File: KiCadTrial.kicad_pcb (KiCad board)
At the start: 2 copper layers, 3 parts, among them J1 Conn_01x02

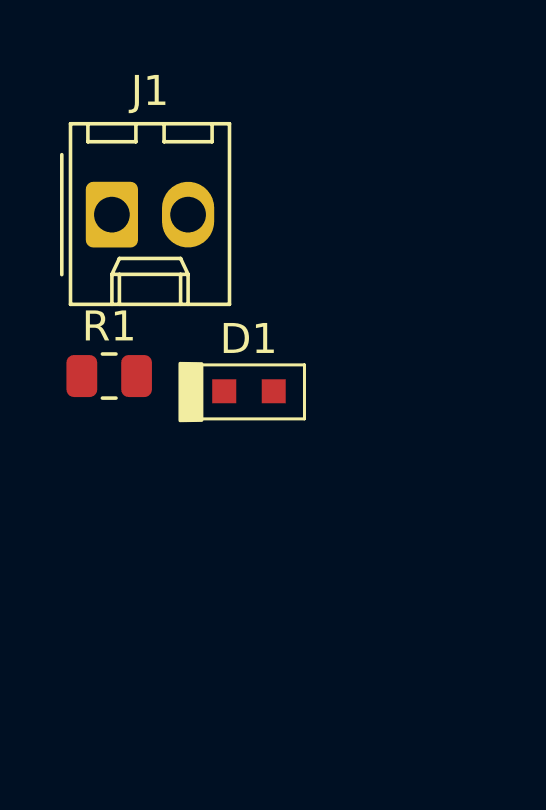
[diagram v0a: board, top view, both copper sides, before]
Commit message: Initial PCB Routing
Placed component on grid.
Routed copper on the front layer.
Defined a board outline.
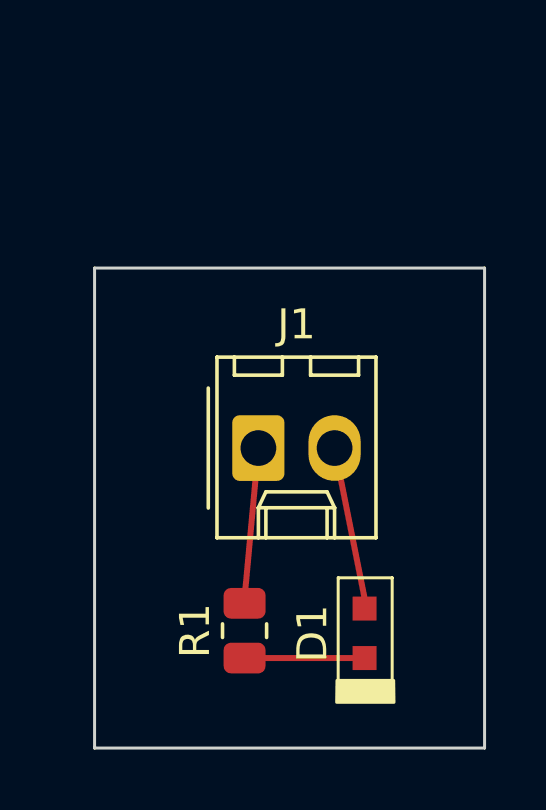
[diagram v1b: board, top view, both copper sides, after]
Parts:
- moved R1 9.61 mm to (156.0, 110.1), turned to 90 degrees
- moved J1 9.19 mm to (156.5, 104.0)
- moved D1 8.94 mm to (160.0, 110.2), turned to 90 degrees
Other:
- board outline added: 13 x 16 mm
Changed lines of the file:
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@@
   (net 3 "+3.3V")
   (footprint "myPCBLib:LED0603" (layer "F.Cu")
-    (at 156.147 102.108)
+    (at 160 110.175 90)
     (descr "Surface Mount LED 0603 - white")
     (tags "optical electronics")
@@
     (property "ki_keywords" "Optoelectronics")
     (attr smd)
-    (fp_text reference "D1" (at -0.01 -1.74 unlocked) (layer "F.SilkS")
+    (fp_text reference "D1" (at -0.01 -1.74 90 unlocked) (layer "F.SilkS")
         (effects (font (size 1 1) (thickness 0.1)))
     )
-    (fp_text value "White" (at 0.03 2.37 unlocked) (layer "F.Fab")
-        (effects (font (size 1 1) (thickness 0.15)))
-    )
-    (fp_text user "REF**" (at -2.11 0.69 unlocked) (layer "F.Fab")
+    (fp_text value "White" (at 0.03 2.37 90 unlocked) (layer "F.Fab")
+        (effects (font (size 1 1) (thickness 0.15)))
+    )
+    (fp_text user "REF**" (at -2.11 0.69 90 unlocked) (layer "F.Fab")
         (effects (font (size 1 1) (thickness 0.15)) (justify left bottom))
     )
-    (fp_text user "${REFERENCE}" (at 0 1.54 unlocked) (layer "F.Fab")
+    (fp_text user "${REFERENCE}" (at 0 1.54 90 unlocked) (layer "F.Fab")
         (effects (font (size 0.5 0.5) (thickness 0.125)))
     )
@@
       )
       (stroke (width 0.1) (type solid)) (fill solid) (layer "F.CrtYd"))
-    (pad "A" smd rect (at 0.825 0) (size 0.8 0.8) (layers "F.Cu" "F.Paste" "F.Mask")
+    (pad "A" smd rect (at 0.825 0 90) (size 0.8 0.8) (layers "F.Cu" "F.Paste" "F.Mask")
       (net 1 "GND") (pinfunction "Anode") (pintype "passive") (thermal_bridge_angle 45))
-    (pad "C" smd rect (at -0.825 0) (size 0.8 0.8) (layers "F.Cu" "F.Paste" "F.Mask")
+    (pad "C" smd rect (at -0.825 0 90) (size 0.8 0.8) (layers "F.Cu" "F.Paste" "F.Mask")
       (net 2 "Net-(D1-Cathode)") (pinfunction "Cathode") (pintype "passive") (thermal_bridge_angle 45))
     (model "${KICAD6_3DMODEL_DIR}/LED_SMD.3dshapes/LED_0603_1608Metric.wrl"
@@
   )
   (footprint "Connector_Molex:Molex_KK-254_AE-6410-02A_1x02_P2.54mm_Vertical" (layer "F.Cu")
-    (at 151.5775 96.22)
+    (at 156.46 104)
     (descr "Molex KK-254 Interconnect System, old/engineering part number: AE-6410-02A example for new part number: 22-27-2021, 2 Pins (http://www.molex.com/pdm_docs/sd/022272021_sd.pdf), generated with kicad-footprint-generator")
     (tags "connector Molex KK-254 vertical")
@@
   )
   (footprint "Resistor_SMD:R_0805_2012Metric" (layer "F.Cu")
-    (at 151.4875 101.6)
+    (at 156 110.0875 90)
     (descr "Resistor SMD 0805 (2012 Metric), square (rectangular) end terminal, IPC_7351 nominal, (Body size source: IPC-SM-782 page 72, https://www.pcb-3d.com/wordpress/wp-content/uploads/ipc-sm-782a_amendment_1_and_2.pdf), generated with kicad-footprint-generator")
     (tags "resistor")
@@
     (property "ki_keywords" "resistor variable light sensitive opto LDR")
     (attr smd)
-    (fp_text reference "R1" (at 0 -1.65) (layer "F.SilkS")
-        (effects (font (size 1 1) (thickness 0.15)))
-    )
-    (fp_text value "R_Photo" (at 0 1.65) (layer "F.Fab")
-        (effects (font (size 1 1) (thickness 0.15)))
-    )
-    (fp_text user "${REFERENCE}" (at 0 0) (layer "F.Fab")
+    (fp_text reference "R1" (at 0 -1.65 90) (layer "F.SilkS")
+        (effects (font (size 1 1) (thickness 0.15)))
+    )
+    (fp_text value "R_Photo" (at 0 1.65 90) (layer "F.Fab")
+        (effects (font (size 1 1) (thickness 0.15)))
+    )
+    (fp_text user "${REFERENCE}" (at 0 0 90) (layer "F.Fab")
         (effects (font (size 0.5 0.5) (thickness 0.08)))
     )
@@
     (fp_line (start 1 0.625) (end -1 0.625)
       (stroke (width 0.1) (type solid)) (layer "F.Fab"))
-    (pad "1" smd roundrect (at -0.9125 0) (size 1.025 1.4) (layers "F.Cu" "F.Paste" "F.Mask") (roundrect_rratio 0.243902)
+    (pad "1" smd roundrect (at -0.9125 0 90) (size 1.025 1.4) (layers "F.Cu" "F.Paste" "F.Mask") (roundrect_rratio 0.243902)
       (net 2 "Net-(D1-Cathode)") (pintype "passive"))
-    (pad "2" smd roundrect (at 0.9125 0) (size 1.025 1.4) (layers "F.Cu" "F.Paste" "F.Mask") (roundrect_rratio 0.243902)
+    (pad "2" smd roundrect (at 0.9125 0 90) (size 1.025 1.4) (layers "F.Cu" "F.Paste" "F.Mask") (roundrect_rratio 0.243902)
       (net 3 "+3.3V") (pintype "passive"))
     (model "${KICAD6_3DMODEL_DIR}/Resistor_SMD.3dshapes/R_0805_2012Metric.wrl"
@@
     )
   )
+  (gr_line (start 160 109) (end 159 104)
+    (stroke (width 0.2) (type default)) (layer "F.Cu"))
+  (gr_line (start 156 109) (end 156.46 104)
+    (stroke (width 0.2) (type default)) (layer "F.Cu"))
+  (gr_line (start 160 111) (end 156 111)
+    (stroke (width 0.2) (type default)) (layer "F.Cu"))
+  (gr_line (start 164 98) (end 164 114)
+    (stroke (width 0.1) (type default)) (layer "Edge.Cuts"))
+  (gr_line (start 164 114) (end 151 114)
+    (stroke (width 0.1) (type default)) (layer "Edge.Cuts"))
+  (gr_line (start 151 114) (end 151 98)
+    (stroke (width 0.1) (type default)) (layer "Edge.Cuts"))
+  (gr_line (start 151 98) (end 164 98)
+    (stroke (width 0.1) (type default)) (layer "Edge.Cuts"))
 )

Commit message: Changes by Lee.
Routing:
- net GND: track 0.00 -> 6.07 mm
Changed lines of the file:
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@@
     )
   )
-  (gr_line (start 160 109) (end 159 104)
-    (stroke (width 0.2) (type default)) (layer "F.Cu"))
   (gr_line (start 156 109) (end 156.46 104)
     (stroke (width 0.2) (type default)) (layer "F.Cu"))
@@
   (gr_line (start 151 98) (end 164 98)
     (stroke (width 0.1) (type default)) (layer "Edge.Cuts"))
+  (segment (start 160.02 104.521) (end 160 104.541) (width 0.25) (layer "F.Cu") (net 1))
+  (segment (start 159.499 104) (end 160.02 104.521) (width 0.25) (layer "F.Cu") (net 1))
+  (segment (start 160 104.541) (end 160 109.35) (width 0.25) (layer "F.Cu") (net 1))
+  (segment (start 159 104) (end 159.499 104) (width 0.25) (layer "F.Cu") (net 1))
 )

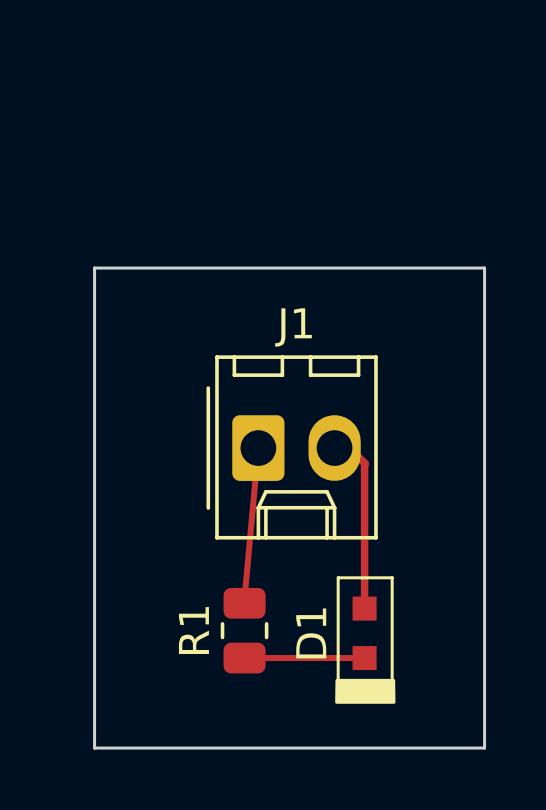
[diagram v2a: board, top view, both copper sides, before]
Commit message: Add ground fill to the Front Copper
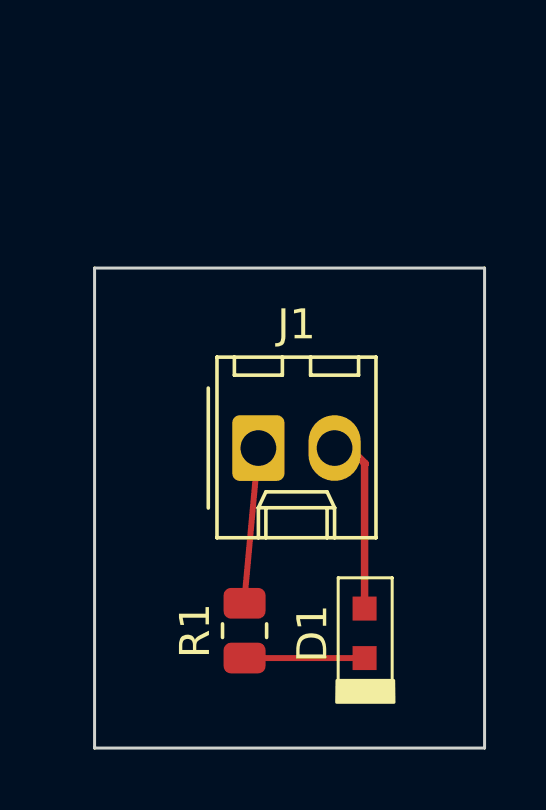
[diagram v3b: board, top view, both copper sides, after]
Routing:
- added copper zone on F.Cu, net GND
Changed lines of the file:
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@@
   (segment (start 160 104.541) (end 160 109.35) (width 0.25) (layer "F.Cu") (net 1))
   (segment (start 159 104) (end 159.499 104) (width 0.25) (layer "F.Cu") (net 1))
+  (zone (net 1) (net_name "GND") (layer "F.Cu") (hatch edge 0.5)
+    (connect_pads (clearance 0.5))
+    (min_thickness 0.25) (filled_areas_thickness no)
+    (fill yes (thermal_gap 0.5) (thermal_bridge_width 0.5))
+    (polygon
+      (pts
+        (xy 151 98)
+        (xy 164 98)
+        (xy 164 114)
+        (xy 151 114)
+      )
+    )
+  )
 )

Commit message: JLCPCB PN
added JLCPCB PN to all components.
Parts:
- R1: value R_Photo -> 330
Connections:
- D1 pad C: Net-(D1-Cathode) -> unconnected-(D1-Cathode-PadC)
- R1 pad 1: Net-(D1-Cathode) -> unconnected-(R1-Pad1)
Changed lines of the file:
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@@
   (net 0 "")
   (net 1 "GND")
-  (net 2 "Net-(D1-Cathode)")
+  (net 2 "unconnected-(D1-Cathode-PadC)")
   (net 3 "+3.3V")
+  (net 4 "unconnected-(R1-Pad1)")
   (footprint "myPCBLib:LED0603" (layer "F.Cu")
     (at 160 110.175 90)
     (descr "Surface Mount LED 0603 - white")
     (tags "optical electronics")
+    (property "JLCPCB" "C965805")
+    (property "MPN" "XL-1608SYGC-06")
+    (property "Manufacturer" "XINGLIGHT")
     (property "PN" "EKT_426738")
     (property "Sheetfile" "KiCadTrial.kicad_sch")
@@
       (net 1 "GND") (pinfunction "Anode") (pintype "passive") (thermal_bridge_angle 45))
     (pad "C" smd rect (at -0.825 0 90) (size 0.8 0.8) (layers "F.Cu" "F.Paste" "F.Mask")
-      (net 2 "Net-(D1-Cathode)") (pinfunction "Cathode") (pintype "passive") (thermal_bridge_angle 45))
+      (net 2 "unconnected-(D1-Cathode-PadC)") (pinfunction "Cathode") (pintype "passive") (thermal_bridge_angle 45))
     (model "${KICAD6_3DMODEL_DIR}/LED_SMD.3dshapes/LED_0603_1608Metric.wrl"
       (offset (xyz 0 0 0))
@@
     (descr "Molex KK-254 Interconnect System, old/engineering part number: AE-6410-02A example for new part number: 22-27-2021, 2 Pins (http://www.molex.com/pdm_docs/sd/022272021_sd.pdf), generated with kicad-footprint-generator")
     (tags "connector Molex KK-254 vertical")
+    (property "JLCPCB" "C5116481")
+    (property "MPN" "2.54-1*2")
+    (property "Manufacturer" "ZHOURI")
+    (property "PN" "anything")
     (property "Sheetfile" "KiCadTrial.kicad_sch")
     (property "Sheetname" "")
@@
     (descr "Resistor SMD 0805 (2012 Metric), square (rectangular) end terminal, IPC_7351 nominal, (Body size source: IPC-SM-782 page 72, https://www.pcb-3d.com/wordpress/wp-content/uploads/ipc-sm-782a_amendment_1_and_2.pdf), generated with kicad-footprint-generator")
     (tags "resistor")
+    (property "JLCPCB" "C23138")
+    (property "MPN" "0603WAF3300T5E")
+    (property "Manufacturer" "UNI-ROYAL(Uniroyal Elec)")
+    (property "PN" "something")
     (property "Sheetfile" "KiCadTrial.kicad_sch")
     (property "Sheetname" "")
@@
         (effects (font (size 1 1) (thickness 0.15)))
     )
-    (fp_text value "R_Photo" (at 0 1.65 90) (layer "F.Fab")
+    (fp_text value "330" (at 0 1.65 90) (layer "F.Fab")
         (effects (font (size 1 1) (thickness 0.15)))
     )
@@
       (stroke (width 0.1) (type solid)) (layer "F.Fab"))
     (pad "1" smd roundrect (at -0.9125 0 90) (size 1.025 1.4) (layers "F.Cu" "F.Paste" "F.Mask") (roundrect_rratio 0.243902)
-      (net 2 "Net-(D1-Cathode)") (pintype "passive"))
+      (net 4 "unconnected-(R1-Pad1)") (pintype "passive"))
     (pad "2" smd roundrect (at 0.9125 0 90) (size 1.025 1.4) (layers "F.Cu" "F.Paste" "F.Mask") (roundrect_rratio 0.243902)
       (net 3 "+3.3V") (pintype "passive"))

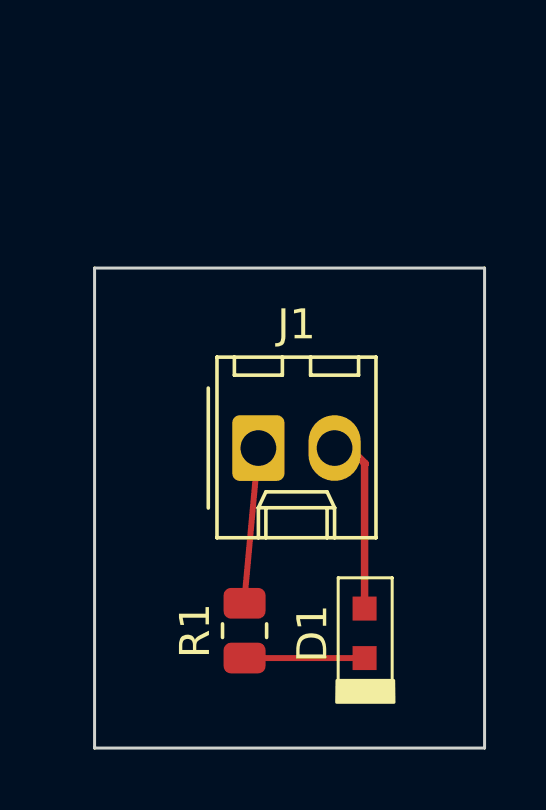
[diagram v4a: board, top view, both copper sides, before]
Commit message: Design for manufacture
Added board description, version, and a space/place for the SN
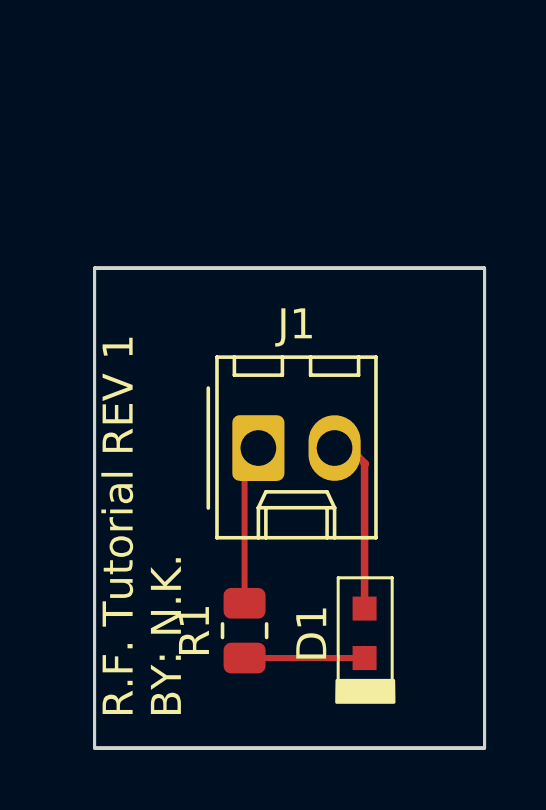
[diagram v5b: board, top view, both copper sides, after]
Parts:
- R1: value 330 -> R_Photo
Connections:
- D1 pad C: unconnected-(D1-Cathode-PadC) -> Net-(D1-Cathode)
- R1 pad 1: unconnected-(R1-Pad1) -> Net-(D1-Cathode)
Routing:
- added copper zone on B.Cu, net GND
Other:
- rule pad_to_mask_clearance: 0 -> 0.1
- board text added: "R.F. Tutorial REV 1 BY: N.K."
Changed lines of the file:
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@@
   (layers
     (0 "F.Cu" signal)
-    (31 "B.Cu" signal)
+    (31 "B.Cu" mixed)
     (32 "B.Adhes" user "B.Adhesive")
     (33 "F.Adhes" user "F.Adhesive")
@@
   )
   (setup
-    (pad_to_mask_clearance 0)
+    (stackup
+      (layer "F.SilkS" (type "Top Silk Screen"))
+      (layer "F.Paste" (type "Top Solder Paste"))
+      (layer "F.Mask" (type "Top Solder Mask") (thickness 0.01))
+      (layer "F.Cu" (type "copper") (thickness 0.035))
+      (layer "dielectric 1" (type "core") (thickness 1.51) (material "FR4") (epsilon_r 4.5) (loss_tangent 0.02))
+      (layer "B.Cu" (type "copper") (thickness 0.035))
+      (layer "B.Mask" (type "Bottom Solder Mask") (thickness 0.01))
+      (layer "B.Paste" (type "Bottom Solder Paste"))
+      (layer "B.SilkS" (type "Bottom Silk Screen"))
+      (copper_finish "None")
+      (dielectric_constraints no)
+      (edge_plating yes)
+    )
+    (pad_to_mask_clearance 0.1)
     (pcbplotparams
       (layerselection 0x00010fc_ffffffff)
@@
       (dashed_line_gap_ratio 3.000000)
       (svgprecision 4)
-      (plotframeref false)
+      (plotframeref true)
       (viasonmask false)
       (mode 1)
@@
       (plotvalue true)
       (plotinvisibletext false)
-      (sketchpadsonfab false)
+      (sketchpadsonfab true)
       (subtractmaskfromsilk false)
       (outputformat 1)
       (mirror false)
-      (drillshape 1)
+      (drillshape 0)
       (scaleselection 1)
-      (outputdirectory "")
+      (outputdirectory "./")
     )
   )
   (net 0 "")
   (net 1 "GND")
-  (net 2 "unconnected-(D1-Cathode-PadC)")
-  (net 3 "+3.3V")
-  (net 4 "unconnected-(R1-Pad1)")
+  (net 2 "+3.3V")
+  (net 3 "Net-(D1-Cathode)")
   (footprint "myPCBLib:LED0603" (layer "F.Cu")
     (at 160 110.175 90)
     (descr "Surface Mount LED 0603 - white")
     (tags "optical electronics")
-    (property "JLCPCB" "C965805")
-    (property "MPN" "XL-1608SYGC-06")
-    (property "Manufacturer" "XINGLIGHT")
     (property "PN" "EKT_426738")
     (property "Sheetfile" "KiCadTrial.kicad_sch")
@@
       (net 1 "GND") (pinfunction "Anode") (pintype "passive") (thermal_bridge_angle 45))
     (pad "C" smd rect (at -0.825 0 90) (size 0.8 0.8) (layers "F.Cu" "F.Paste" "F.Mask")
-      (net 2 "unconnected-(D1-Cathode-PadC)") (pinfunction "Cathode") (pintype "passive") (thermal_bridge_angle 45))
+      (net 3 "Net-(D1-Cathode)") (pinfunction "Cathode") (pintype "passive") (thermal_bridge_angle 45))
     (model "${KICAD6_3DMODEL_DIR}/LED_SMD.3dshapes/LED_0603_1608Metric.wrl"
       (offset (xyz 0 0 0))
@@
     (descr "Molex KK-254 Interconnect System, old/engineering part number: AE-6410-02A example for new part number: 22-27-2021, 2 Pins (http://www.molex.com/pdm_docs/sd/022272021_sd.pdf), generated with kicad-footprint-generator")
     (tags "connector Molex KK-254 vertical")
-    (property "JLCPCB" "C5116481")
-    (property "MPN" "2.54-1*2")
-    (property "Manufacturer" "ZHOURI")
-    (property "PN" "anything")
     (property "Sheetfile" "KiCadTrial.kicad_sch")
     (property "Sheetname" "")
@@
     (fp_line (start 3.81 2.88) (end 3.81 -2.92)
       (stroke (width 0.1) (type solid)) (layer "F.Fab"))
-    (pad "1" thru_hole roundrect (at 0 0) (size 1.74 2.19) (drill 1.19) (layers "*.Cu" "*.Mask") (roundrect_rratio 0.143678)
-      (net 3 "+3.3V") (pinfunction "Pin_1") (pintype "passive"))
+    (pad "1" thru_hole roundrect (at 0 0) (size 1.74 2.19) (drill 1.19) (layers "*.Cu" "*.Mask") (roundrect_rratio 0.1436781609)
+      (net 2 "+3.3V") (pinfunction "Pin_1") (pintype "passive"))
     (pad "2" thru_hole oval (at 2.54 0) (size 1.74 2.19) (drill 1.19) (layers "*.Cu" "*.Mask")
       (net 1 "GND") (pinfunction "Pin_2") (pintype "passive"))
@@
     (descr "Resistor SMD 0805 (2012 Metric), square (rectangular) end terminal, IPC_7351 nominal, (Body size source: IPC-SM-782 page 72, https://www.pcb-3d.com/wordpress/wp-content/uploads/ipc-sm-782a_amendment_1_and_2.pdf), generated with kicad-footprint-generator")
     (tags "resistor")
-    (property "JLCPCB" "C23138")
-    (property "MPN" "0603WAF3300T5E")
-    (property "Manufacturer" "UNI-ROYAL(Uniroyal Elec)")
-    (property "PN" "something")
     (property "Sheetfile" "KiCadTrial.kicad_sch")
     (property "Sheetname" "")
@@
         (effects (font (size 1 1) (thickness 0.15)))
     )
-    (fp_text value "330" (at 0 1.65 90) (layer "F.Fab")
+    (fp_text value "R_Photo" (at 0 1.65 90) (layer "F.Fab")
         (effects (font (size 1 1) (thickness 0.15)))
     )
@@
     (fp_line (start 1 0.625) (end -1 0.625)
       (stroke (width 0.1) (type solid)) (layer "F.Fab"))
-    (pad "1" smd roundrect (at -0.9125 0 90) (size 1.025 1.4) (layers "F.Cu" "F.Paste" "F.Mask") (roundrect_rratio 0.243902)
-      (net 4 "unconnected-(R1-Pad1)") (pintype "passive"))
-    (pad "2" smd roundrect (at 0.9125 0 90) (size 1.025 1.4) (layers "F.Cu" "F.Paste" "F.Mask") (roundrect_rratio 0.243902)
-      (net 3 "+3.3V") (pintype "passive"))
+    (pad "1" smd roundrect (at -0.9125 0 90) (size 1.025 1.4) (layers "F.Cu" "F.Paste" "F.Mask") (roundrect_rratio 0.243902439)
+      (net 3 "Net-(D1-Cathode)") (pintype "passive"))
+    (pad "2" smd roundrect (at 0.9125 0 90) (size 1.025 1.4) (layers "F.Cu" "F.Paste" "F.Mask") (roundrect_rratio 0.243902439)
+      (net 2 "+3.3V") (pintype "passive"))
     (model "${KICAD6_3DMODEL_DIR}/Resistor_SMD.3dshapes/R_0805_2012Metric.wrl"
       (offset (xyz 0 0 0))
@@
     )
   )
-  (gr_line (start 156 109) (end 156.46 104)
+  (gr_line (start 156 109) (end 156 105)
     (stroke (width 0.2) (type default)) (layer "F.Cu"))
   (gr_line (start 160 111) (end 156 111)
@@
   (gr_line (start 151 114) (end 151 98)
     (stroke (width 0.1) (type default)) (layer "Edge.Cuts"))
+  (gr_poly
+    (pts
+      (xy 151 98)
+      (xy 164 98)
+      (xy 164 114)
+      (xy 151 114)
+    )
+    (stroke (width 0.1) (type solid)) (fill none) (layer "Edge.Cuts"))
   (gr_line (start 151 98) (end 164 98)
     (stroke (width 0.1) (type default)) (layer "Edge.Cuts"))
+  (gr_text "R.F. Tutorial REV 1\nBY: N.K. \n" (at 154 113 90) (layer "F.SilkS")
+    (effects (font (size 1 1) (thickness 0.15)) (justify left bottom))
+  )
+  (gr_text_box "SN___________"
+    (start 161 114) (end 164 98) (angle 90) (layer "F.SilkS")
+      (effects (font (size 1 1) (thickness 0.15)) (justify left top))
+    (stroke (width 0.15) (type solid))  )
   (segment (start 160.02 104.521) (end 160 104.541) (width 0.25) (layer "F.Cu") (net 1))
   (segment (start 159.499 104) (end 160.02 104.521) (width 0.25) (layer "F.Cu") (net 1))
@@
     (connect_pads (clearance 0.5))
     (min_thickness 0.25) (filled_areas_thickness no)
+    (fill yes (thermal_gap 0.5) (thermal_bridge_width 0.5))
+    (polygon
+      (pts
+        (xy 151 98)
+        (xy 164 98)
+        (xy 164 114)
+        (xy 151 114)
+      )
+    )
+  )
+  (zone (net 1) (net_name "GND") (layer "B.Cu") (hatch edge 0.5)
+    (priority 1)
+    (connect_pads (clearance 0.5))
+    (min_thickness 0.25) (filled_areas_thickness no)
